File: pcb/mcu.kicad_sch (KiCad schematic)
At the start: 8 parts

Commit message: finish mcu :-)
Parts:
- added C? (x6): 100n, symbol Device:C
- added C? (x2): 10u, symbol Device:C_Polarized_US
- C? (x2): value C -> 12p
- C?: value C -> 1u
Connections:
- net +3.3V: now also C?.1, C?.1, C?.1, C?.1, C?.1; no longer U?.K8 (AVDD_2), U?.K9 (AVDD_1), U?.L10 (AVDD_0)
- net GND: now also U?.C7 (VSS), U?.D4 (VSS), U?.F9 (VSS_DREG), U?.G3 (VSS), U?.G9 (VSS), U?.H6 (VSS), U?.K4 (VSS), U?.L7 (AVSS_2), C?.2, C?.2, C?.2, C?.2, C?.2, C?.2, C?.2, C?.2
- net +3.3VA: now reaches U?.F8 (VDD_DREG)
- net +3.3VA: now also U?.K8 (AVDD_2), U?.K9 (AVDD_1), U?.L10 (AVDD_0), C?.1, C?.1, C?.1
- net må vi spesifisere noe her?: no longer names the net of C?.1, U?.F11 (DECOUPLE)
- no-connect marks 19 -> 75

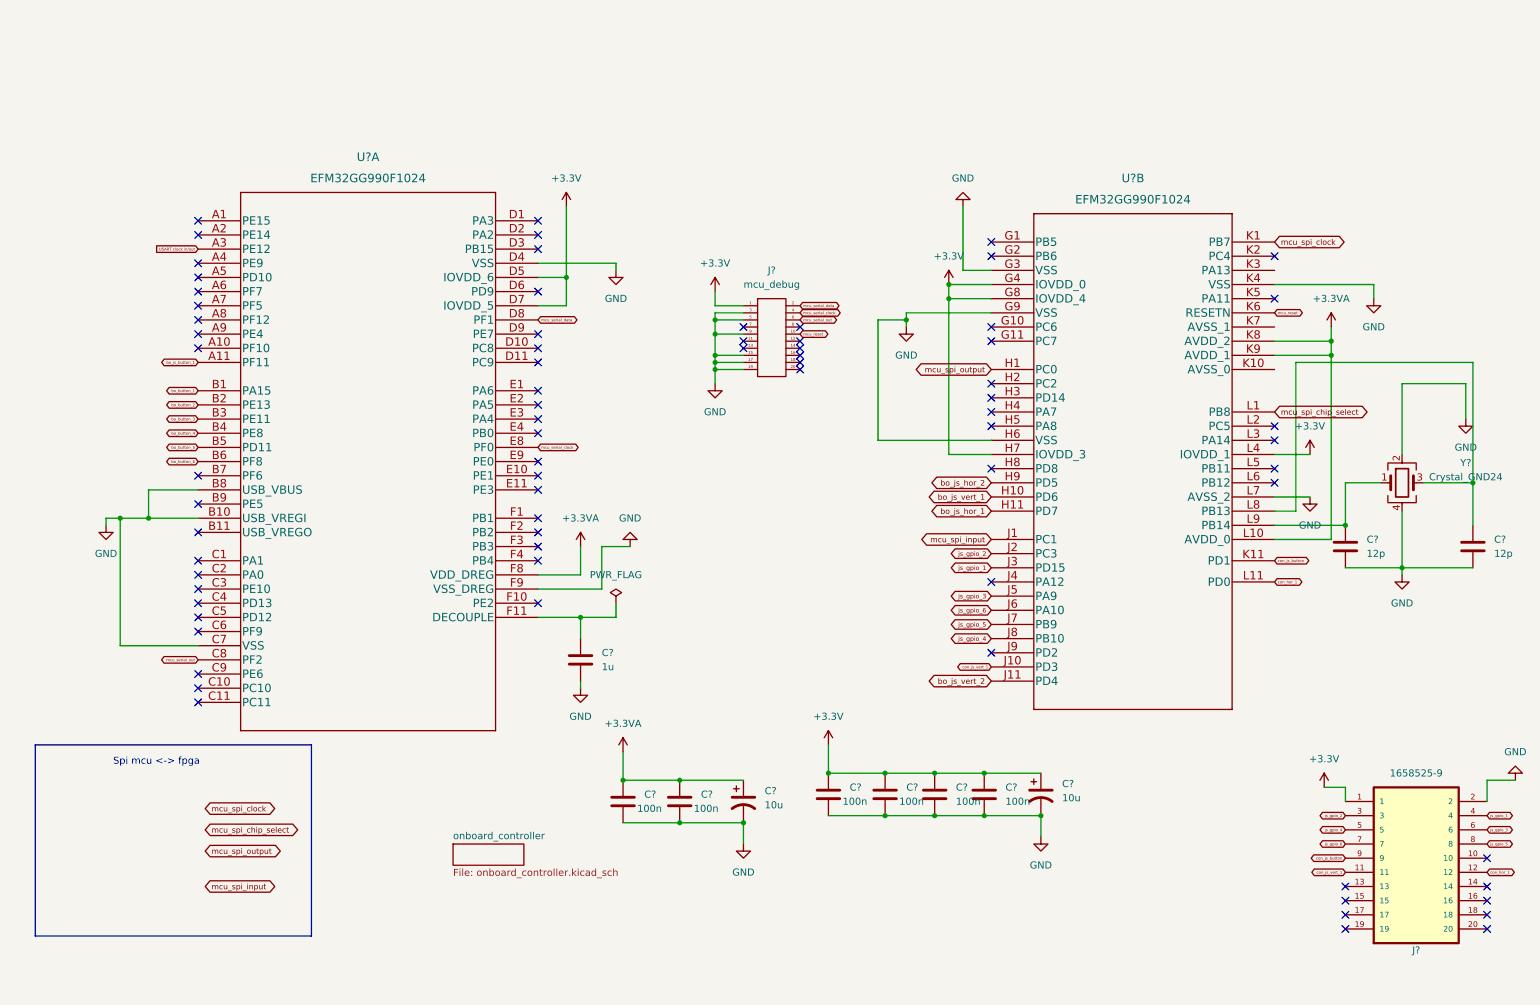
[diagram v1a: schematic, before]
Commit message: add vga
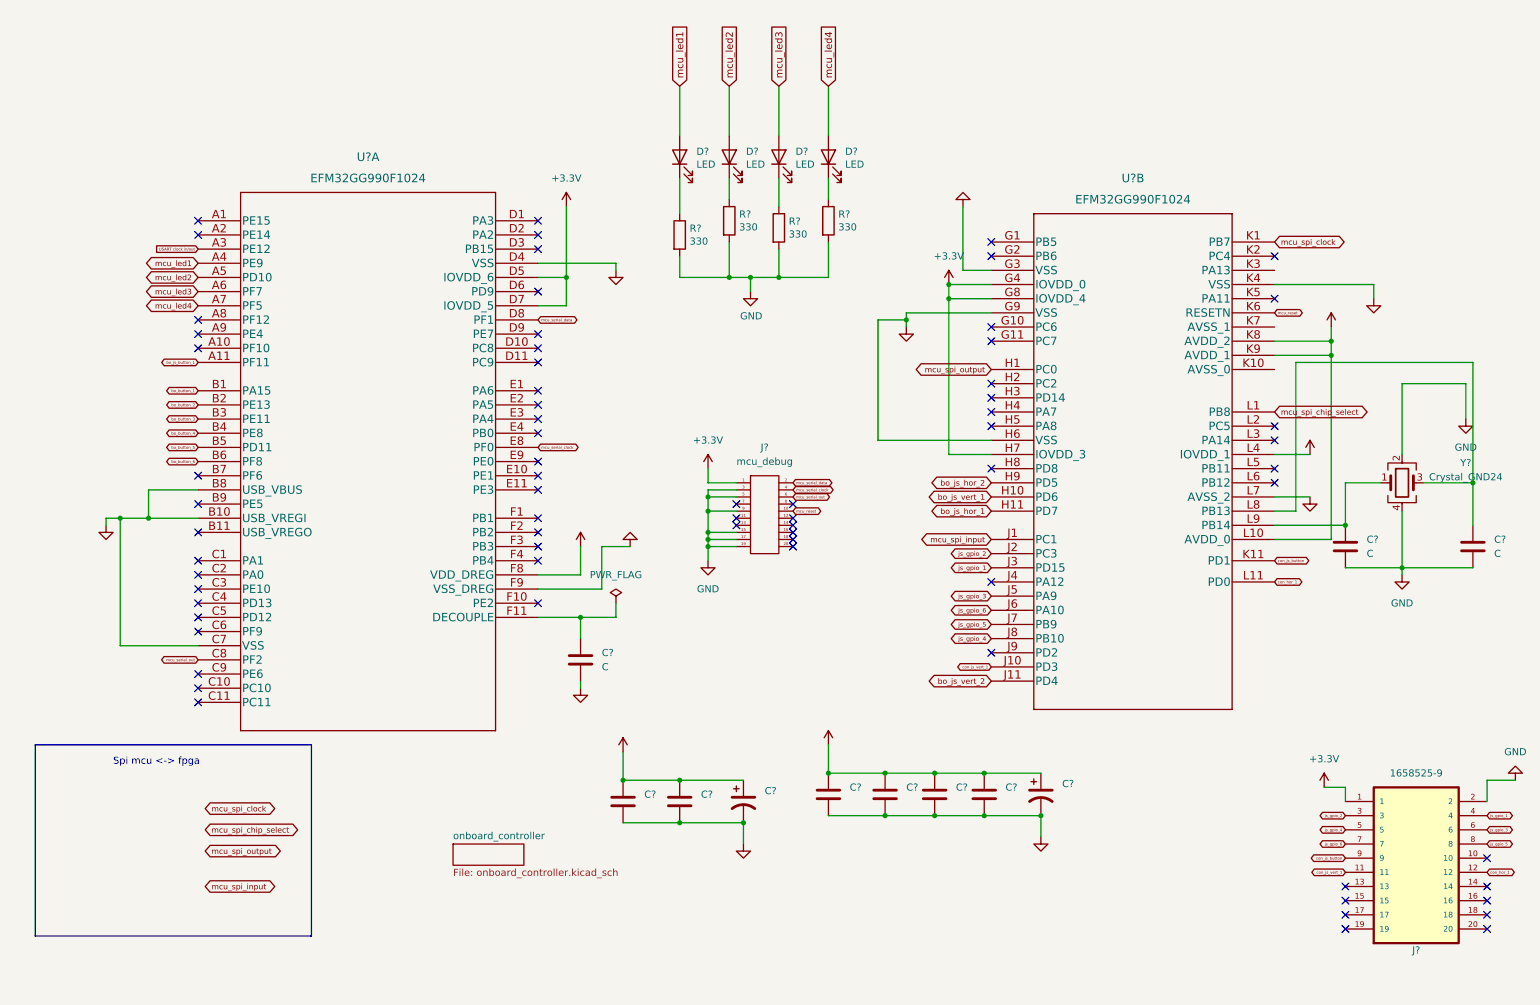
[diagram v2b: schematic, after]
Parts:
- added D? (x4): LED, LED_SMD:LED_1206_3216Metric_Pad1.42x1.75mm_HandSolder, symbol Device:LED
- added R? (x4): 330, Resistor_SMD:R_2512_6332Metric_Pad1.40x3.35mm_HandSolder, symbol Device:R
- C? (x2): value 12p -> C
- C? (x6): value 100n -> (none)
- C? (x2): value 10u -> (none)
- C?: value 1u -> C
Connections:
- net GND: now also R?.2, R?.2, R?.2, R?.2
- net mcu_led1: now reaches U?.A4 (PE9)
- net mcu_led1: now also D?.2 (A)
- net mcu_led2: now reaches U?.A5 (PD10)
- net mcu_led2: now also D?.2 (A)
- net mcu_led3: now reaches U?.A6 (PF7)
- net mcu_led3: now also D?.2 (A)
- net mcu_led4: now reaches U?.A7 (PF5)
- net mcu_led4: now also D?.2 (A)
- new net: D?.1 (K), R?.1 (x4)
- no-connect marks 75 -> 71
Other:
- moved on the sheet: J?

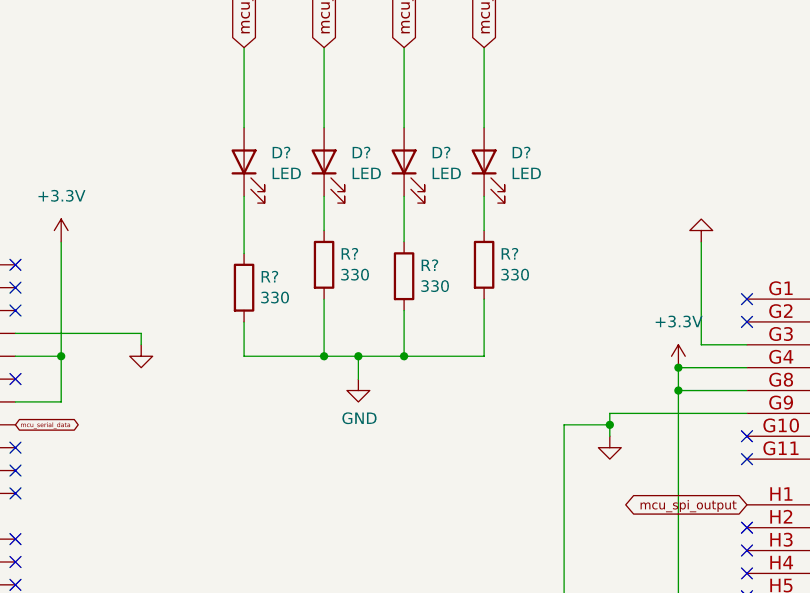
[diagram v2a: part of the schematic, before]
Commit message: added new_vga and sram
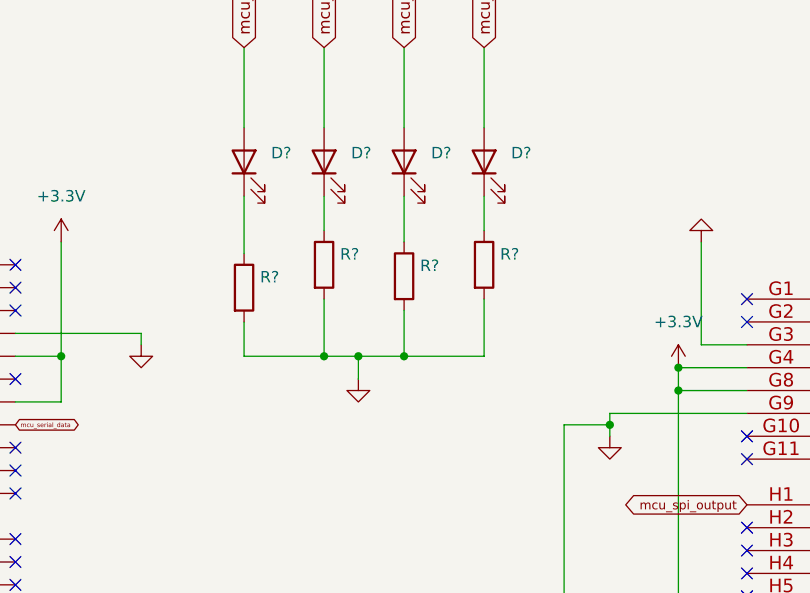
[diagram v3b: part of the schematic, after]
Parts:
- C? (x8): value (none) -> ~
- D? (x4): value LED -> (none); footprint LED_SMD:LED_1206_3216Metric_Pad1.42x1.75mm_HandSolder -> (none)
- R? (x4): value 330 -> (none); footprint Resistor_SMD:R_2512_6332Metric_Pad1.40x3.35mm_HandSolder -> (none)

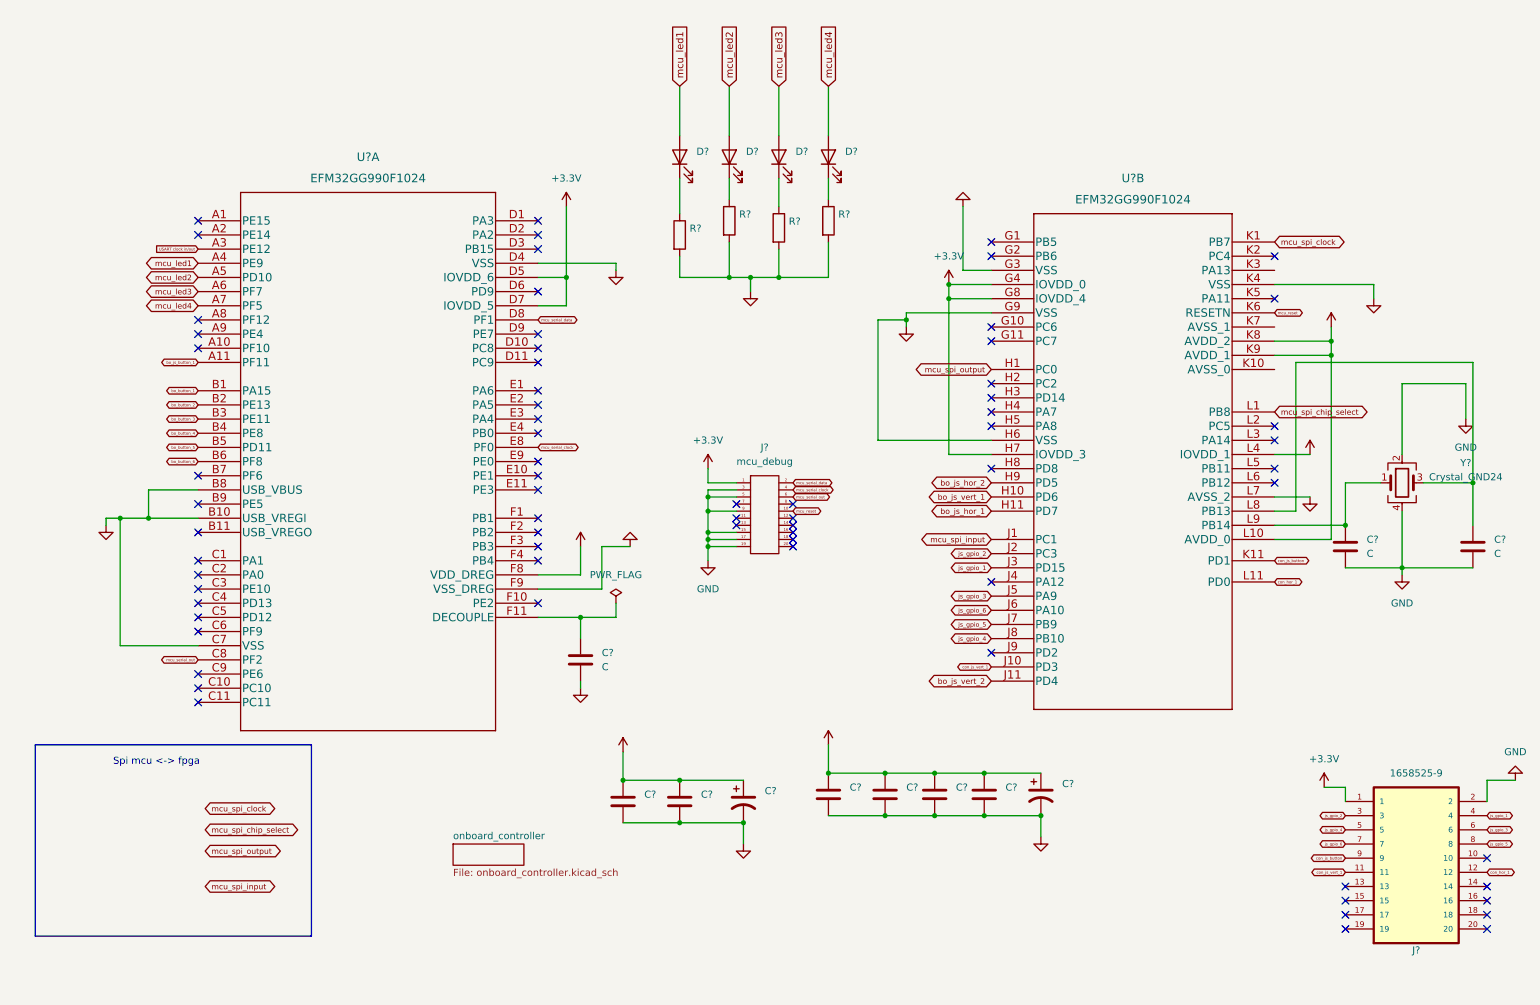
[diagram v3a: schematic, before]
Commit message: connect sram and vga to fpga
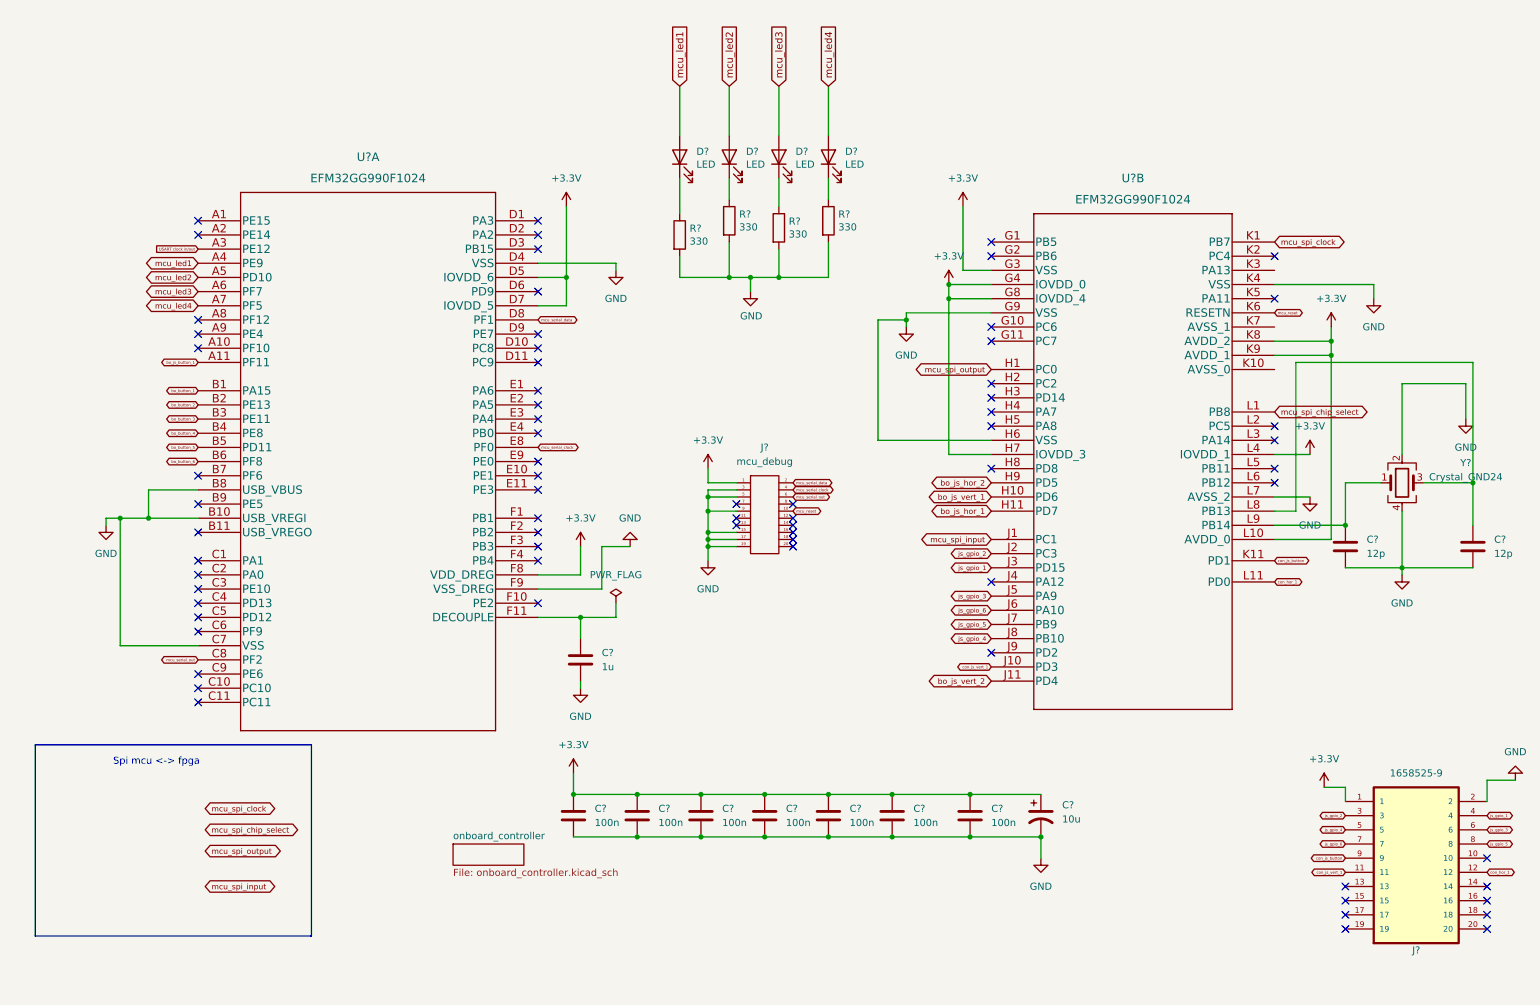
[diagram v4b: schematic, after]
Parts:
- removed C? (x6): ~, symbol Device:C
- removed C? (x2): ~, symbol Device:C_Polarized_US
- added C? (x7): 100n, symbol Device:C
- added C?: 10u, symbol Device:C_Polarized_US
- C? (x2): value C -> 12p
- C?: value C -> 1u
- D? (x4): value (none) -> LED; footprint (none) -> LED_SMD:LED_1206_3216Metric_Pad1.42x1.75mm_HandSolder
- R? (x4): value (none) -> 330; footprint (none) -> Resistor_SMD:R_2512_6332Metric_Pad1.40x3.35mm_HandSolder
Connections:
- net +3.3VA is gone; now on net +3.3V: U?.F8 (VDD_DREG), U?.K8 (AVDD_2), U?.K9 (AVDD_1), U?.L10 (AVDD_0)
- net +3.3V: now also U?.G3 (VSS), C?.1, C?.1, C?.1, C?.1, C?.1, C?.1, C?.1, C?.1
- net GND: now also C?.2, C?.2, C?.2, C?.2, C?.2, C?.2, C?.2, C?.2; no longer U?.G3 (VSS)
